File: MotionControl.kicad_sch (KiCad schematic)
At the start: 25 parts, among them J2 Conn_ARM_JTAG_SWD_10, Q1 2N7002, SW1 SW_Push, U1 ATSAMD21J18A-A, U7 TC4427, Y1 32.768kHz

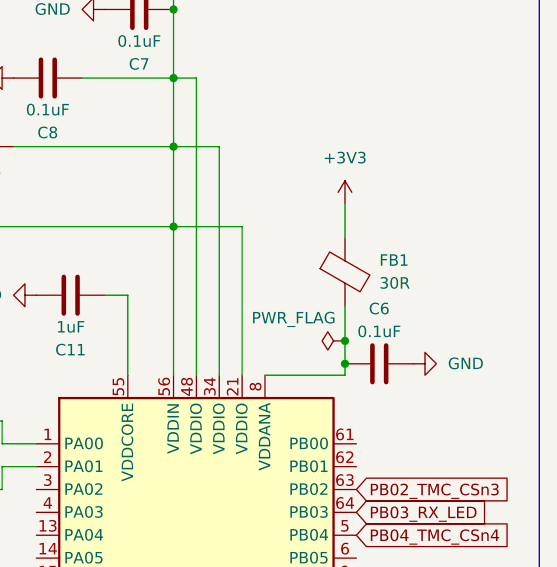
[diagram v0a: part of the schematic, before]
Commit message: Updated footprints, digikey parts
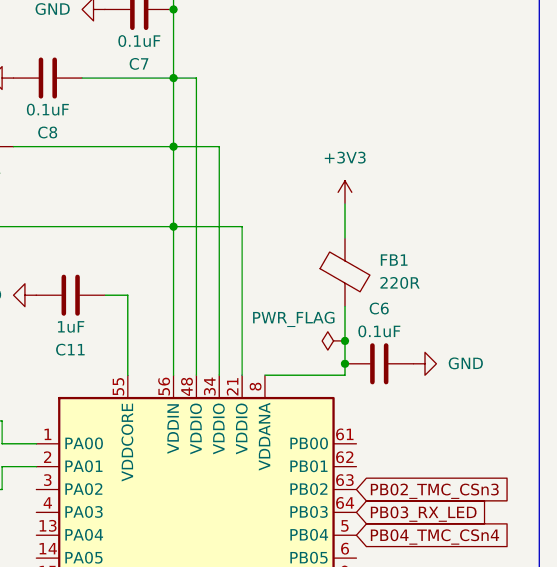
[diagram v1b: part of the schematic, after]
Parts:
- FB1: value 30R -> 220R; Part (none) -> MPZ1608S221ATA00
- Q1: Part (none) -> 2N7002
- U7: Part (none) -> TC4427ACOA713
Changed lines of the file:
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@@
+			)
+		)
+		(property "Part" "2N7002"
+			(at 36.83 36.83 0)
+			(effects
+				(font
+					(size 1.27 1.27)
+				)
+				(hide yes)
 			)
 		)
@@
 			)
 		)
-		(property "Value" "30R"
+		(property "Value" "220R"
 			(at 266.7 50.7491 0)
 			(effects
@@
 		)
 		(property "Description" "Ferrite bead"
+			(at 262.89 49.53 0)
+			(effects
+				(font
+					(size 1.27 1.27)
+				)
+				(hide yes)
+			)
+		)
+		(property "Part" "MPZ1608S221ATA00"
 			(at 262.89 49.53 0)
 			(effects
@@
 			(at 69.85 104.14 0)
 			(effects
+				(font
+					(size 1.27 1.27)
+				)
+				(hide yes)
+			)
+		)
+		(property "Part" "TC4427ACOA713"
+			(at 69.85 104.14 0)
+			(effects
